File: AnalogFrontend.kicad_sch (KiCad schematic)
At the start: 33 parts, among them U1 EL817S1C(F), U6 RS321BXF, U8 RS321BXF

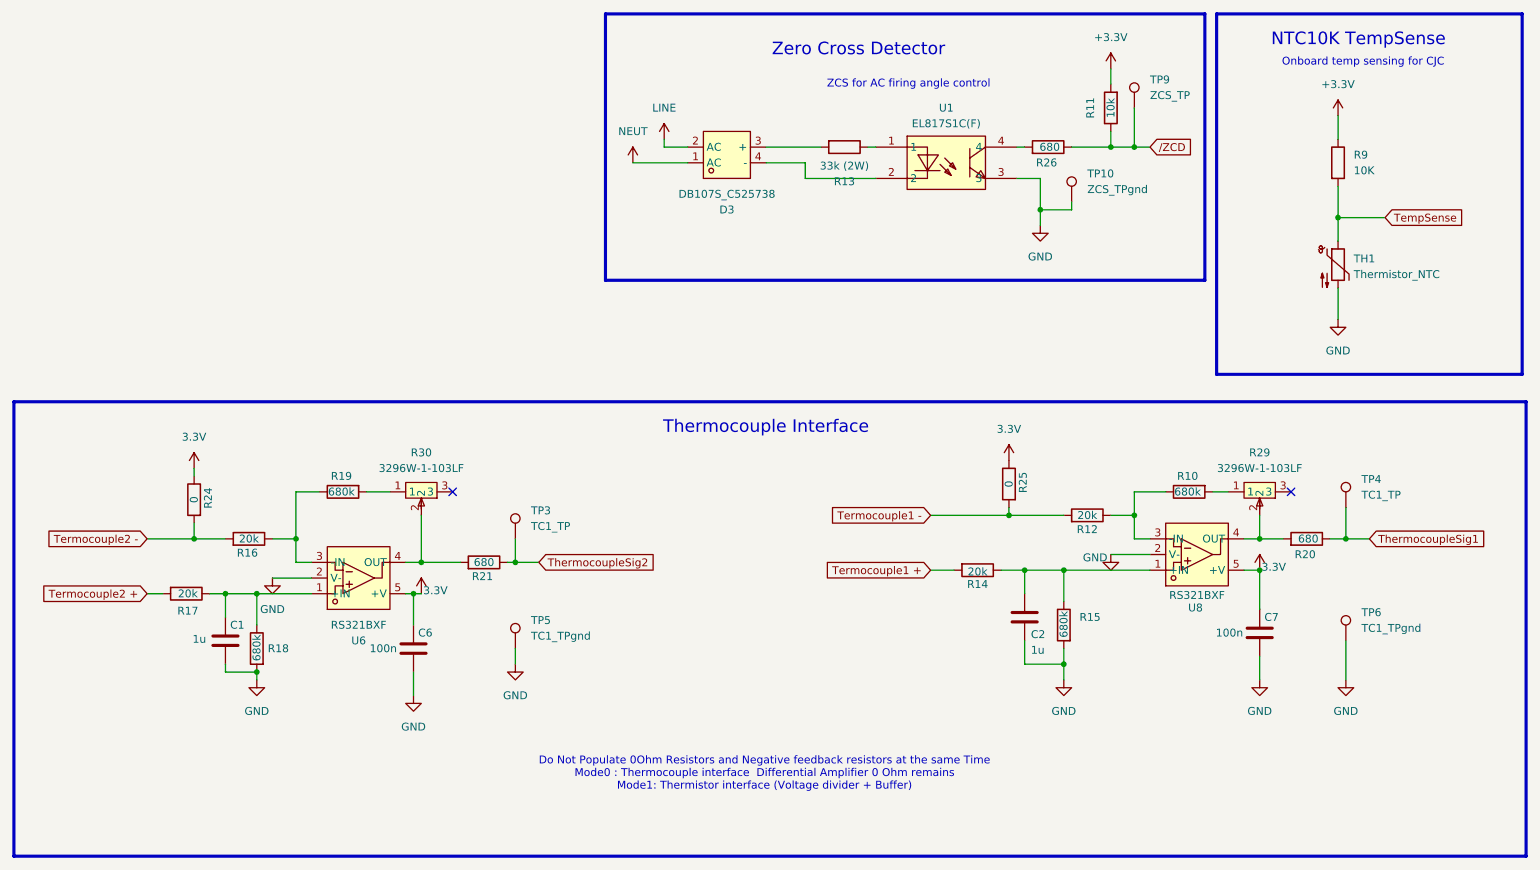
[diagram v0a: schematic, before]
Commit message: Finished Routing, Finished Schematic
Yet to add , solderMask
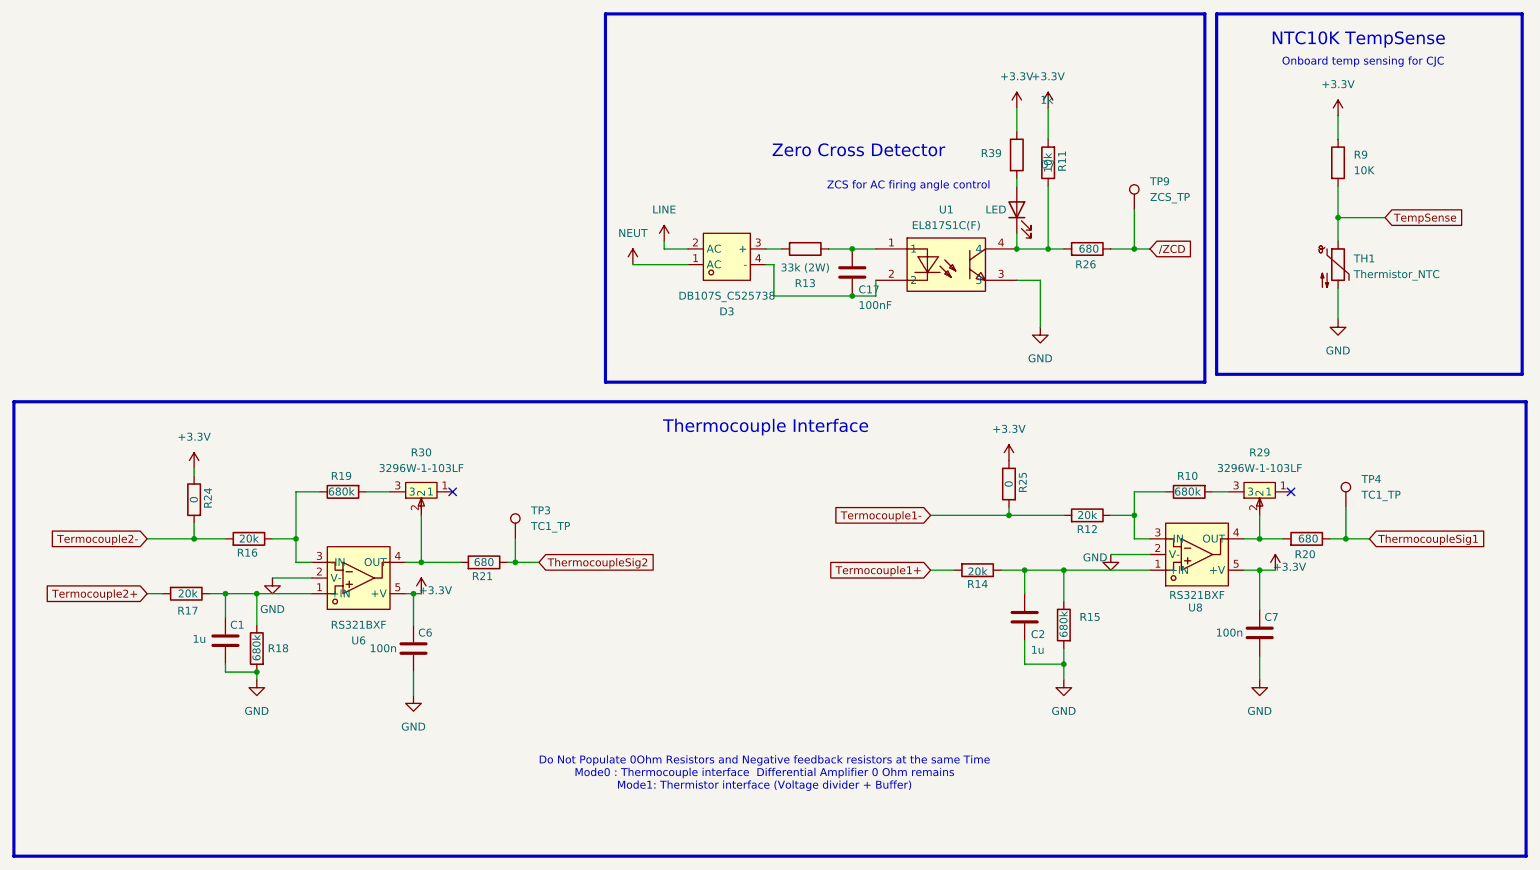
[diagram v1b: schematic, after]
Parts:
- removed TP10: ZCS_TPgnd, TestPoint:TestPoint_THTPad_2.0x2.0mm_Drill1.0mm, symbol Connector:TestPoint
- removed TP5, TP6: TC1_TPgnd, TestPoint:TestPoint_THTPad_2.0x2.0mm_Drill1.0mm, symbol Connector:TestPoint
- added C17: 100nF, Capacitor_SMD:C_1206_3216Metric_Pad1.33x1.80mm_HandSolder, symbol Device:C
- added D7: LED, LED_SMD:LED_1206_3216Metric_Pad1.42x1.75mm_HandSolder, symbol Device:LED
- added R39: 1k, Resistor_SMD:R_1206_3216Metric_Pad1.30x1.75mm_HandSolder, symbol Device:R
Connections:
- net 3.3V is gone; now on net +3.3V: C6.1, C7.1, R24.1, R25.1, U6.5 (+V), U8.5 (+V)
- net +3.3V: now also R39.1
- net /ZCD: no longer R11.1
- net at R29.1: no longer R10.2
- net at R29.3: now also R10.2
- net at D3.4 (-), U1.2: now also C17.2
- net at R13.1, U1.1: now also C17.1
- net at R26.2, U1.4: now also R11.1, D7.1 (K)
- net at R19.2: now also R30.3; no longer R30.1
- net Termocouple1 + renamed Termocouple1+
- net Termocouple1 - renamed Termocouple1-
- net Termocouple2 + renamed Termocouple2+
- net Termocouple2 - renamed Termocouple2-
- new net: D7.2 (A), R39.2
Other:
- moved on the sheet: D3, R11, R13, R26, R29, R30, TP9, U1

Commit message: Fixed Silkscreen, Added production files
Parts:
- renumbered C1 to C14, C6 to C15, C17 to C16, C2 to C17, C7 to C18, D3 to D8, D7 to D9, R17 to R23, R16 to R25, R18 to R26, R19 to R27, R30 to R28, R21 to R29, R13 to R30, R14 to R31, R25 to R32, R39 to R33, R11 to R34, R15 to R35, R26 to R36, R12 to R37, R10 to R38, R29 to R39, R20 to R40, R9 to R41, TP3 to TP5, TP9 to TP6, TP4 to TP7, U6 to U13, U1 to U14, U8 to U15

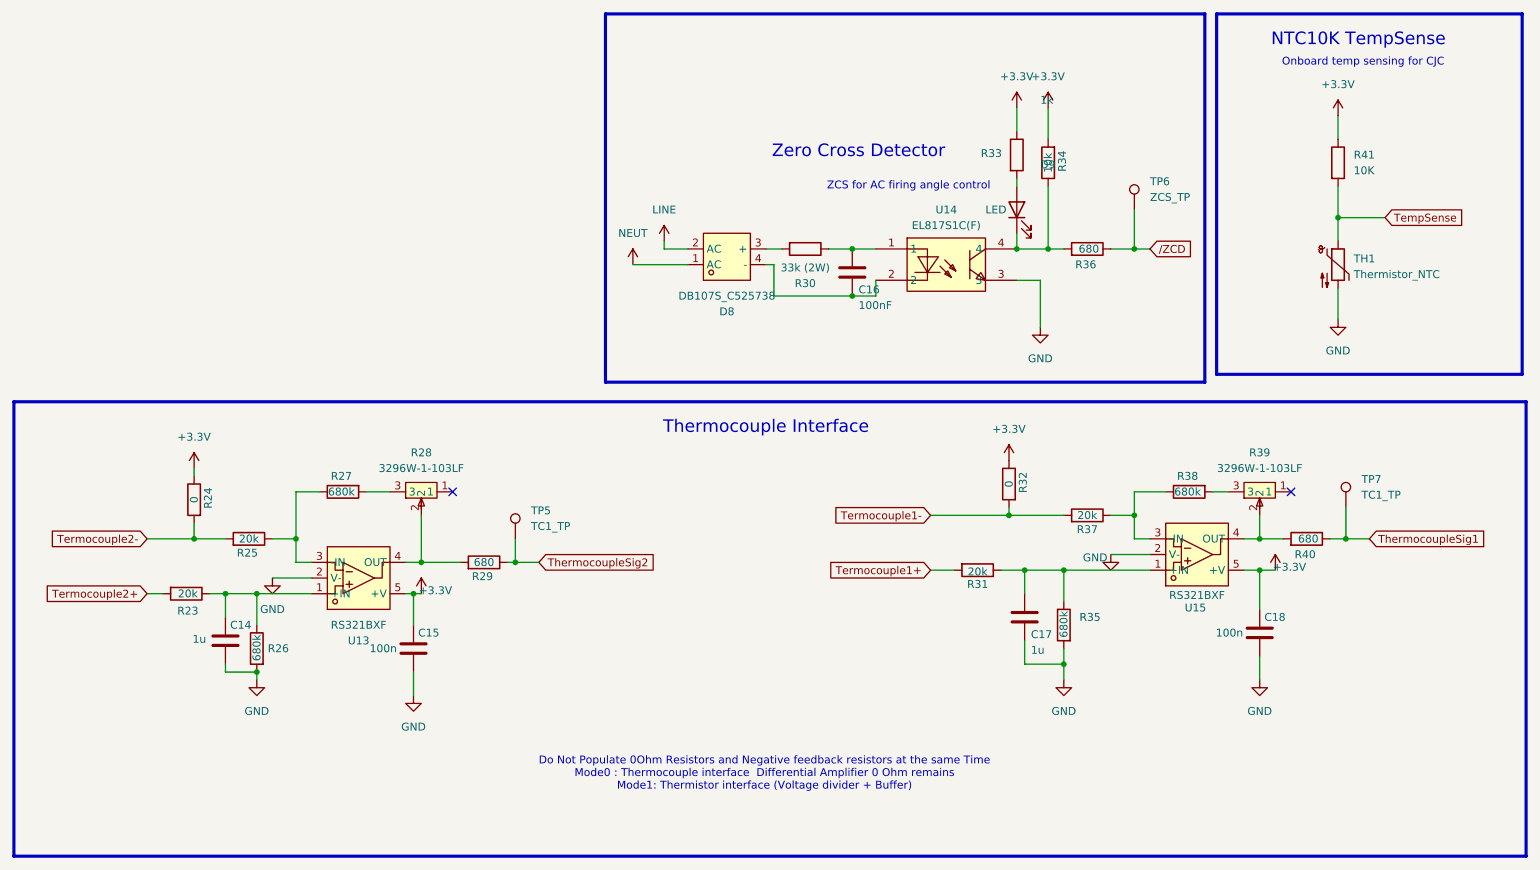
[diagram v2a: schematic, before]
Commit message: Key Fixes and upgrade to V0.1
Design reliance on dedicated thermocouple interface chip instead of calibrating adc and differential amplifier ; Neater routing ; Logos ; High voltage spacing for AC part
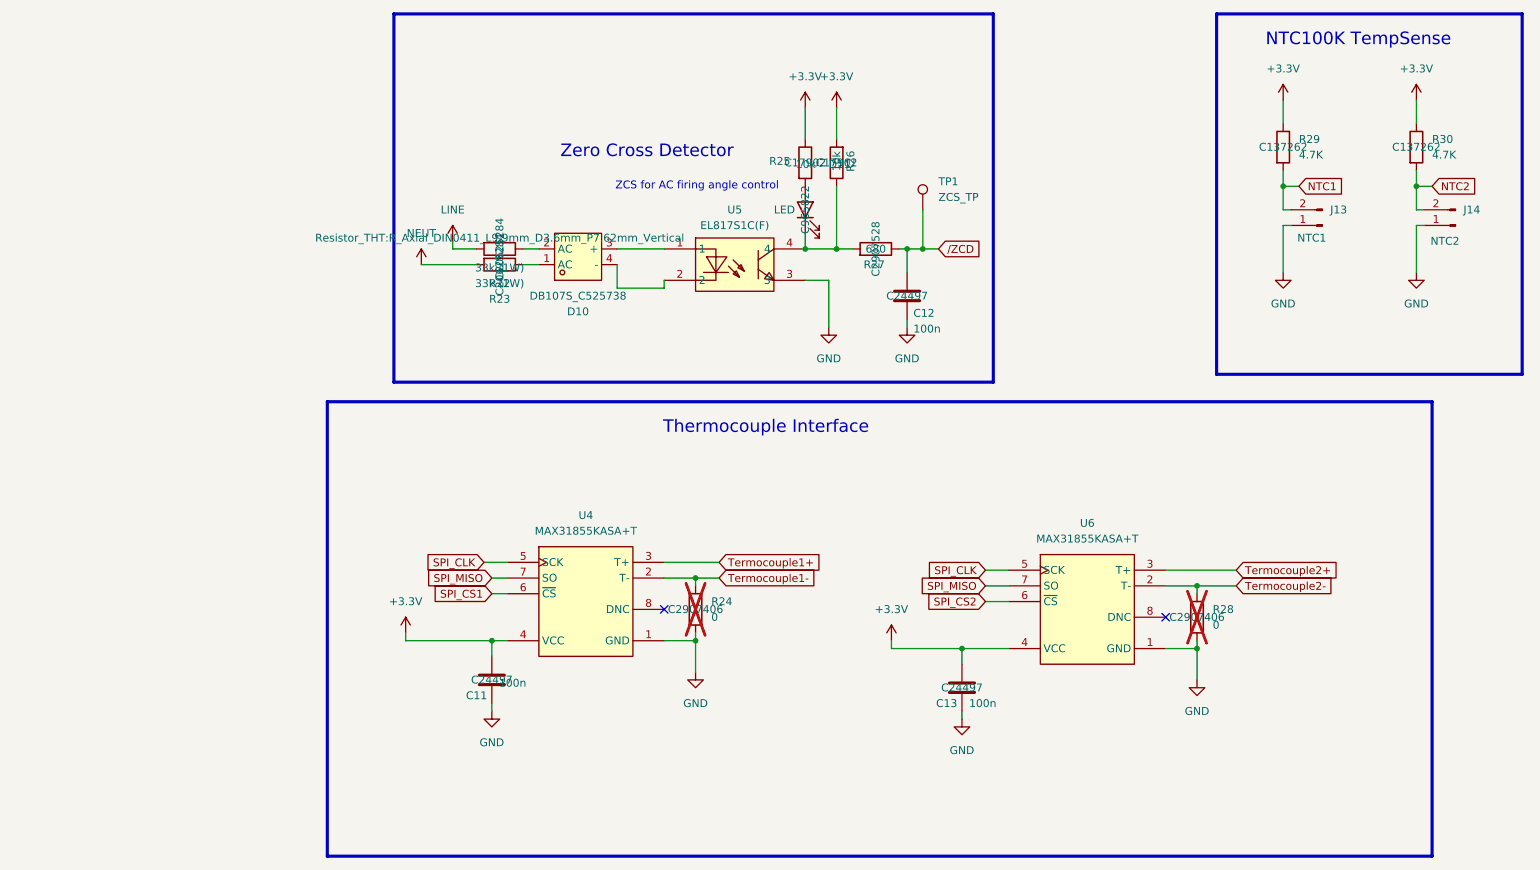
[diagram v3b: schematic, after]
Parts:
- removed C14, C17: 1u, Capacitor_SMD:C_1206_3216Metric_Pad1.33x1.80mm_HandSolder, symbol Device:C
- removed C15, C18: 100n, Capacitor_SMD:C_1206_3216Metric_Pad1.33x1.80mm_HandSolder, symbol Device:C
- removed R23, R25, R31, R37: 20k, Resistor_SMD:R_1206_3216Metric_Pad1.30x1.75mm_HandSolder, symbol Device:R
- removed R26, R27, R35, R38: 680k, Resistor_SMD:R_1206_3216Metric_Pad1.30x1.75mm_HandSolder, symbol Device:R
- removed R28, R39: 3296W-1-103LF, EasyEDA:RES-ADJ-TH_3296W, symbol EasyEDA:3296W-1-103LF
- removed R32: 0, Resistor_SMD:R_1206_3216Metric_Pad1.30x1.75mm_HandSolder, symbol Device:R
- removed R40: 680, Resistor_SMD:R_1206_3216Metric_Pad1.30x1.75mm_HandSolder, symbol Device:R
- removed TH1: Thermistor_NTC, Resistor_THT:R_Axial_DIN0207_L6.3mm_D2.5mm_P2.54mm_Vertical, symbol Device:Thermistor_NTC
- removed TP5, TP7: TC1_TP, TestPoint:TestPoint_THTPad_2.0x2.0mm_Drill1.0mm, symbol Connector:TestPoint
- removed U13, U15: RS321BXF, EasyEDA:SOT-23-5_L2.9-W1.6-P0.95-LS2.8-BL, symbol EasyEDA:RS321BXF
- added C11, C13: 100n, Capacitor_SMD:C_1206_3216Metric_Pad1.33x1.80mm_HandSolder, symbol Device:C
- added J13: NTC1, Connector_PinHeader_2.54mm:PinHeader_1x02_P2.54mm_Vertical, symbol Connector:Conn_01x02_Pin
- added J14: NTC2, Connector_PinHeader_2.54mm:PinHeader_1x02_P2.54mm_Vertical, symbol Connector:Conn_01x02_Pin
- added R22: 33k (1W), Resistor_THT:R_Axial_DIN0411_L9.9mm_D3.6mm_P7.62mm_Vertical, symbol Device:R
- added R28: 0, Resistor_SMD:R_1206_3216Metric_Pad1.30x1.75mm_HandSolder, symbol Device:R
- added U4, U6: MAX31855KASA+T, EasyEDA:SO-8_L4.9-W3.9-P1.27-LS5.9-BL, symbol EasyEDA:MAX31855KASA+T
- C12: renamed from C16; value 100nF -> 100n; LCSC Part (none) -> C24497
- D11: renamed from D9; LCSC Part (none) -> C965822
- R23: renamed from R30; value 33k (2W) -> 33k (1W); footprint Resistor_THT:R_Axial_DIN0414_L11.9mm_D4.5mm_P15.24mm_Horizontal -> Resistor_THT:R_Axial_DIN0411_L9.9mm_D3.6mm_P7.62mm_Vertical; LCSC Part (none) -> C20625284
- R24: LCSC Part (none) -> C2907406; now not fitted
- R25: renamed from R33; value 1k -> 10k; LCSC Part (none) -> C17902
- R26: renamed from R34; LCSC Part (none) -> C17902
- R27: renamed from R36; LCSC Part (none) -> C2907528
- R29: value 680 -> 4.7K; LCSC Part (none) -> C137262
- R30: renamed from R41; value 10K -> 4.7K; LCSC Part (none) -> C137262
- TP1: renamed from TP6; now left out of the parts list
- renumbered D8 to D10, U14 to U5
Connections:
- net ThermocoupleSig2 is gone; now on net +3.3V: R29.1
- net +3.3V: now also C11.2, C13.2, U4.4 (VCC), U6.4 (VCC); no longer R24.1
- net GND: now also C12.2, R24.2, C11.1, C13.1, J13.1 (Pin_1), J14.1 (Pin_1), R28.2, U4.1 (GND), U6.1 (GND)
- net LINE: now also R22.2; no longer D10.2 (AC)
- net NEUT: now also R23.2; no longer D10.1 (AC)
- net Termocouple1+: now also U4.3 (T+)
- net Termocouple1-: now also R24.1, U4.2 (T-)
- net Termocouple2+: now also U6.3 (T+)
- net Termocouple2-: now also R28.1, U6.2 (T-); no longer R24.2
- net /ZCD: now also C12.1
- net at D10.3 (+): now also U5.1; no longer R23.2
- net at D10.4 (-), U5.2: no longer C12.2
- net NTC1: now reaches R29.2
- net NTC1: now also J13.2 (Pin_2)
- net TempSense renamed NTC2
- net NTC2: now also J14.2 (Pin_2)
- new net: D10.1 (AC), R23.1
- new net: D10.2 (AC), R22.1
- new net SPI_CLK: U4.5 (SCK), U6.5 (SCK)
- new net SPI_CS1: U4.6 (~{CS})
- new net SPI_CS2: U6.6 (~{CS})
- new net SPI_MISO: U4.7 (SO), U6.7 (SO)
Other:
- note added: "NTC100K TempSense"
- note removed: "Do Not Populate 0Ohm Resistors and Negative feedback resistors at the same Time Mode0 : Thermocouple interface Differential Amplifier 0 Ohm remains Mode1: Thermistor interface (Voltage divider + Buffer)"
- note removed: "NTC10K TempSense"
- note removed: "Onboard temp sensing for CJC"
- moved on the sheet: C12, D10, D11, R23, R25, R26, R27, R30, TP1, U5
